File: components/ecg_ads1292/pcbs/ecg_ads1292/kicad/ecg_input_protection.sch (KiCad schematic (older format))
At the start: 24 parts

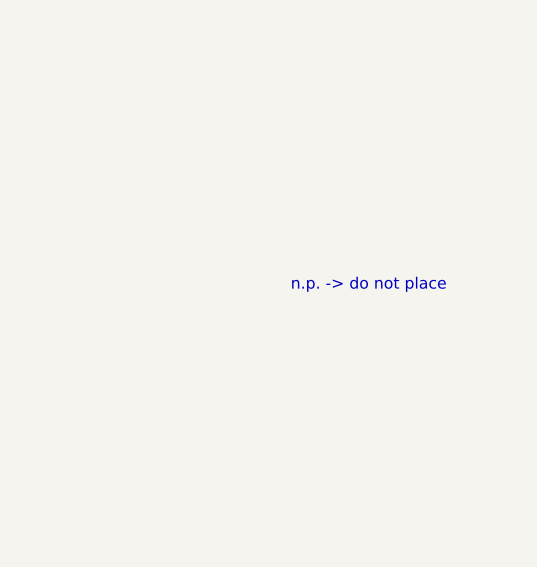
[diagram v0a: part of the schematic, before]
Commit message: add version and titles to schematic pages
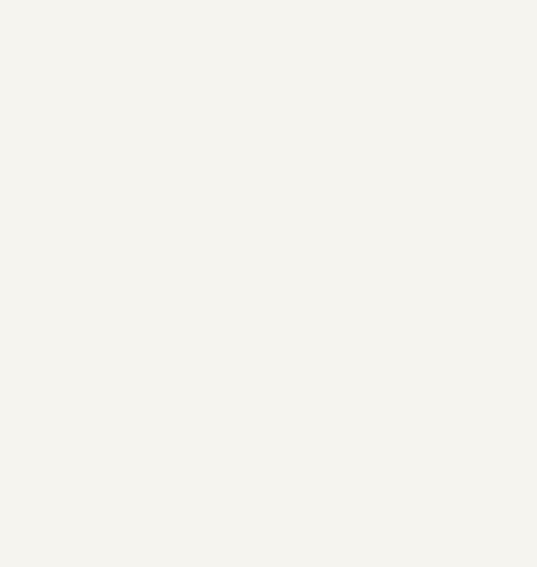
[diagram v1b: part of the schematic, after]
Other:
- note removed: "n.p. -> do not place"
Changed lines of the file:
@@
 encoding utf-8
 Sheet 2 3
-Title "ECG Defibrillator Input Protection"
+Title "Lifesensor acg_ads1292 Defibrillator Input Protection"
 Date "2020-03-28"
-Rev "0"
-Comp "Cadus e.V."
-Comment1 ""
+Rev "0.1"
+Comp "Cadus"
+Comment1 "n.p.: do not place"
 Comment2 ""
 Comment3 ""
@@
 Wire Wire Line
 	2450 5850 4000 5850
-Text Notes 8650 2300 0    50   ~ 0
-n.p. -> do not place
 Text Notes 1350 3350 0    50   ~ 10
 5kV isolation
